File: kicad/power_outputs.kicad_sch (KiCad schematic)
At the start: 36 parts, among them J7 J7 5V out, J8 J8 V_INPUT out, Q3 SI2305A, Q4 MMBT3904, Q5 DMP4015SSS-13, Q6 MMBT3904, Q7 SI2305A, Q8 MMBT3904, U7 INA226 (0x40), U8 INA226 (0x41)

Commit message: Pick JLCPCB parts for the whole BOM and add BOM/CPL generation
Adds bom/parts.csv (LCSC numbers and MPNs), scripts to apply it to the schematic and
board and to generate the JLCPCB BOM, CPL and a live stock report. Swaps the
BOOTSEL/RESET switch to a basic 5.1 mm part with a matching footprint, and replaces
out-of-stock parts (SS54, WS2812B, 10u caps, SWD header).

Co-Authored-By: Claude Sonnet 5.5 <noreply@anthropic.com>
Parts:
- C44, C45: LCSC (none) -> C307331; MPN (none) -> CL05B104KB54PNC
- D5, D7: LCSC C3757794 -> C22452; MPN SS54-HF -> SS54
- R22, R28, R33: LCSC (none) -> C25792; MPN (none) -> 0402WGF4702TCE
- R23, R24, R26, R30, R34, R35: LCSC (none) -> C25744; MPN (none) -> 0402WGF1002TCE
- R25, R31, R36: LCSC (none) -> C25741; MPN (none) -> 0402WGF1003TCE
- R29: LCSC (none) -> C31850; MPN (none) -> 0603WAF2202T5E
- R32: LCSC (none) -> C25768; MPN (none) -> 0402WGF2202TCE
- R37: LCSC (none) -> C25117; MPN (none) -> 0402WGF4700TCE

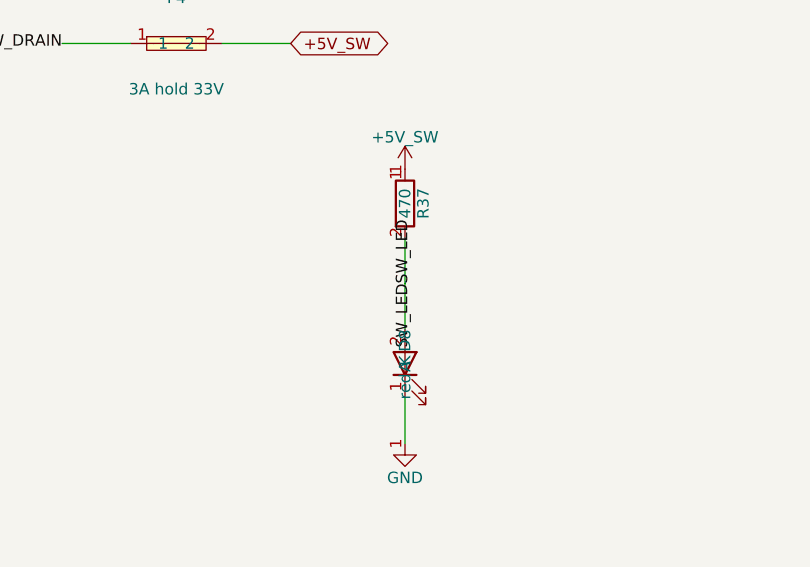
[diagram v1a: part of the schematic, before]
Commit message: Rework board layout, swap SWD header to through-hole, add Qwiic port
- SWD (J10) is now a 1x3 2.54 mm through-hole pin header footprint
  (SWCLK, GND, SWDIO) instead of the JST SH connector; removed from the
  JLCPCB BOM.
- Add J20 Qwiic connector (XY-SM04B-SRSS-TB) on the I2C bus: GND, +3V3,
  GPIO20 (SDA), GPIO21 (SCL), mounting tabs to GND.
- Placement/routing progress and the helper scripts used for it.

DRC still reports open items (unrouted RUN/GPIO24/GPIO29/QSPI_SD0 nets,
R108/GPIO23 and NT1/GPIO20 shorts, J12 edge clearance, silkscreen
overlaps); to be fixed in follow-up commits.

Co-Authored-By: Claude Sonnet 5.5 <noreply@anthropic.com>
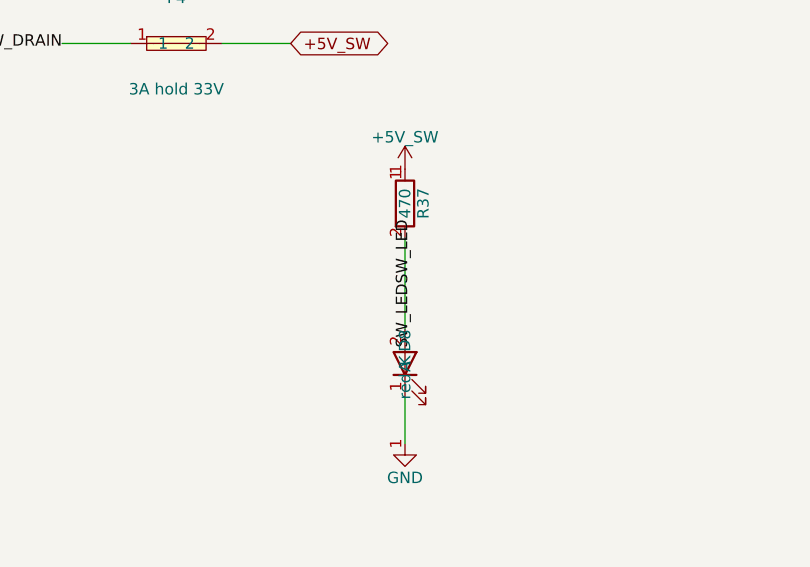
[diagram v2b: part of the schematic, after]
